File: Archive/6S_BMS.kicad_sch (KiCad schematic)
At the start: 48 parts, among them J1 JST_EH_B7B-EH-A, J2 BM06B-GHS-TBT, J3 Conn_ARM_SWD_TagConnect_TC203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, J4 JST_EH_B4B-EH-A, J5 JST_EH_B4B-EH-A, J6 JST_EH_B2B-EH-A, SW1 SW_SPST, U1 BQ76925RGER, U2 STM32L431KCUx, U5 TLV75533PDBV

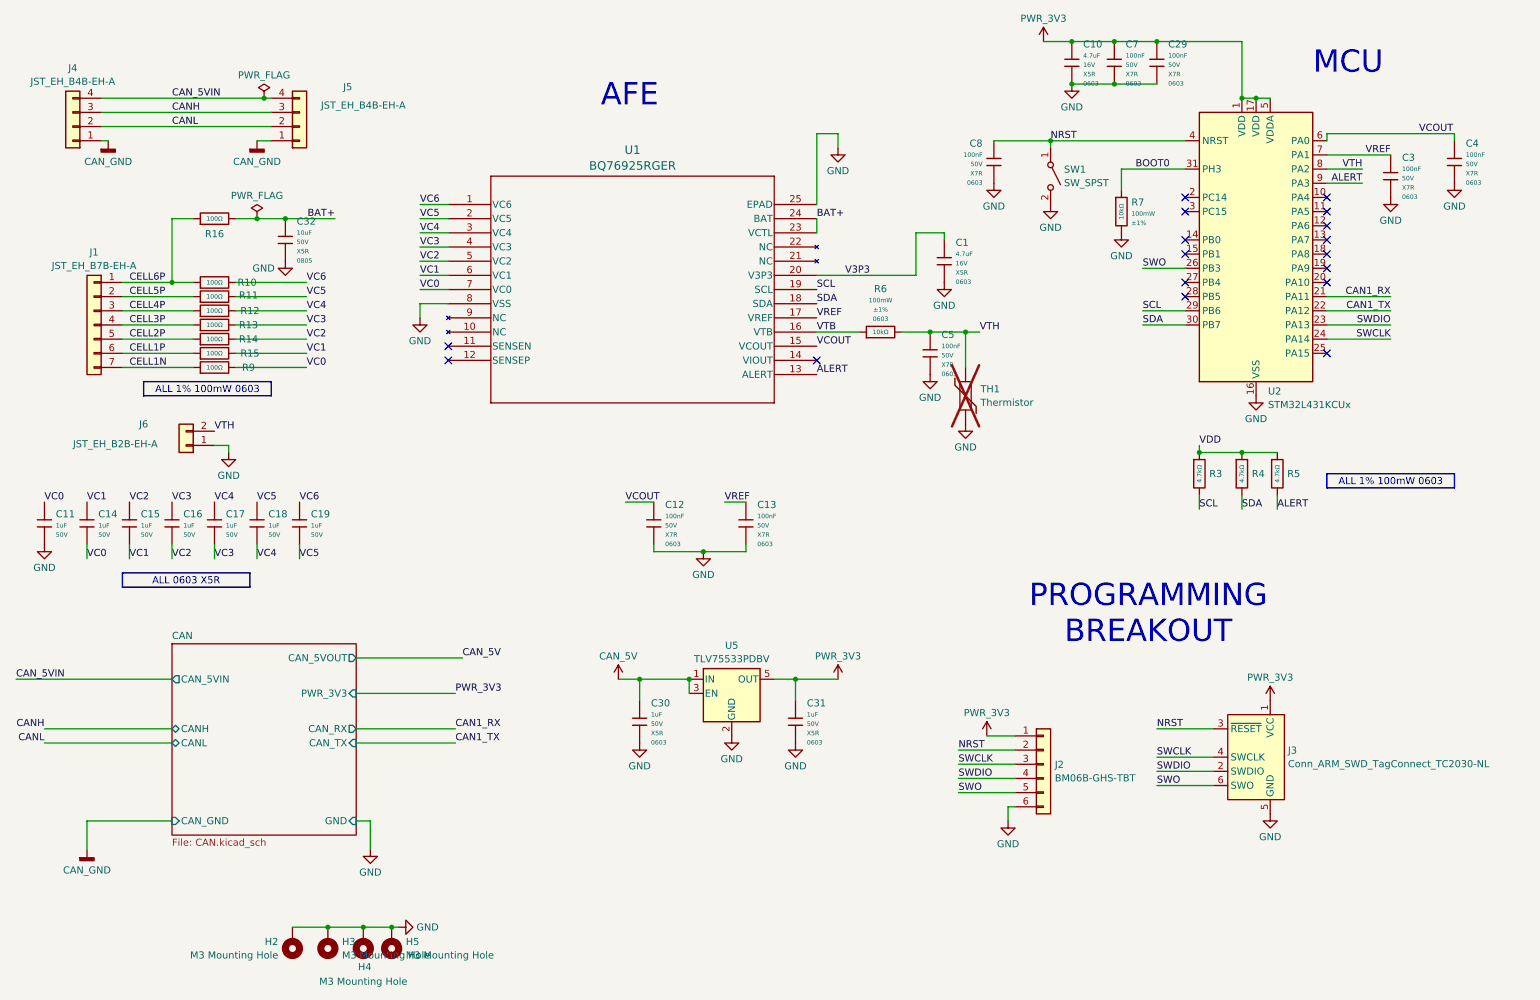
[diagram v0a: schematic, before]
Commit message: Switched to Altium, completed and ordered design
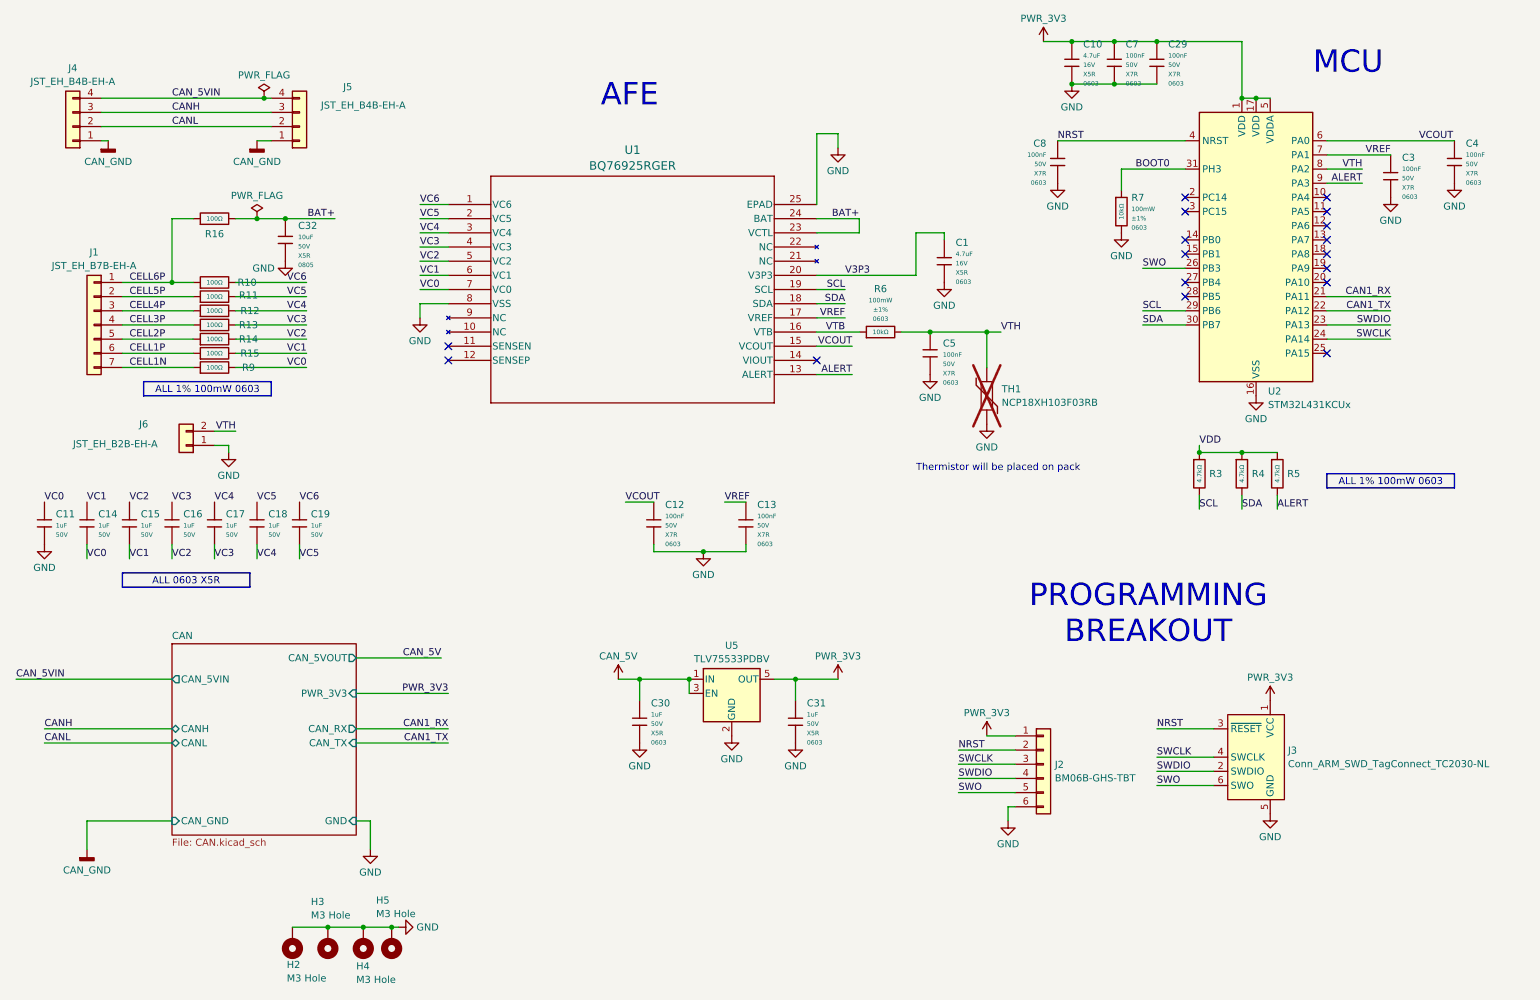
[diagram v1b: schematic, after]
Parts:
- removed SW1: SW_SPST, symbol Switch:SW_SPST
- H2, H3, H4, H5: value M3 Mounting Hole -> M3 Hole
- R7: Package (none) -> 0603
- TH1: value Thermistor -> NCP18XH103F03RB
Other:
- note added: "Thermistor will be placed on pack"
- moved on the sheet: C8, TH1
